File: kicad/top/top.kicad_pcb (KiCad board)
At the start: 2 copper layers, 65 x 120 mm, 32 parts, among them J1 OLED_128x64, J2 Conn_01x15, SW1 SLW-864574-5A-RA-N-D, SW2 RotaryEncoder_Switch

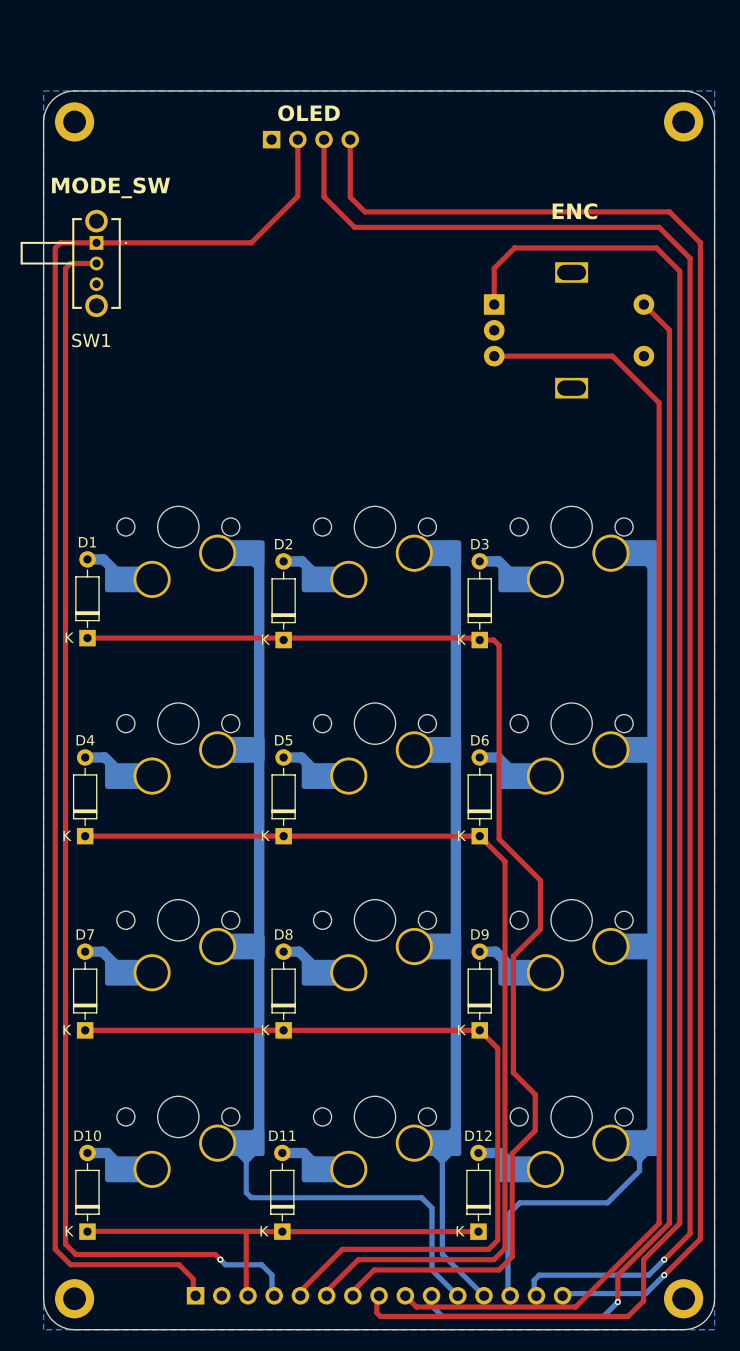
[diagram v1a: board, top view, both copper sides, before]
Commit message: Changed from Adafruit Feather V2 to UnkownMaker ProS3 [D] for USB HID feature. Changed OLED from 128x64 to 128x32
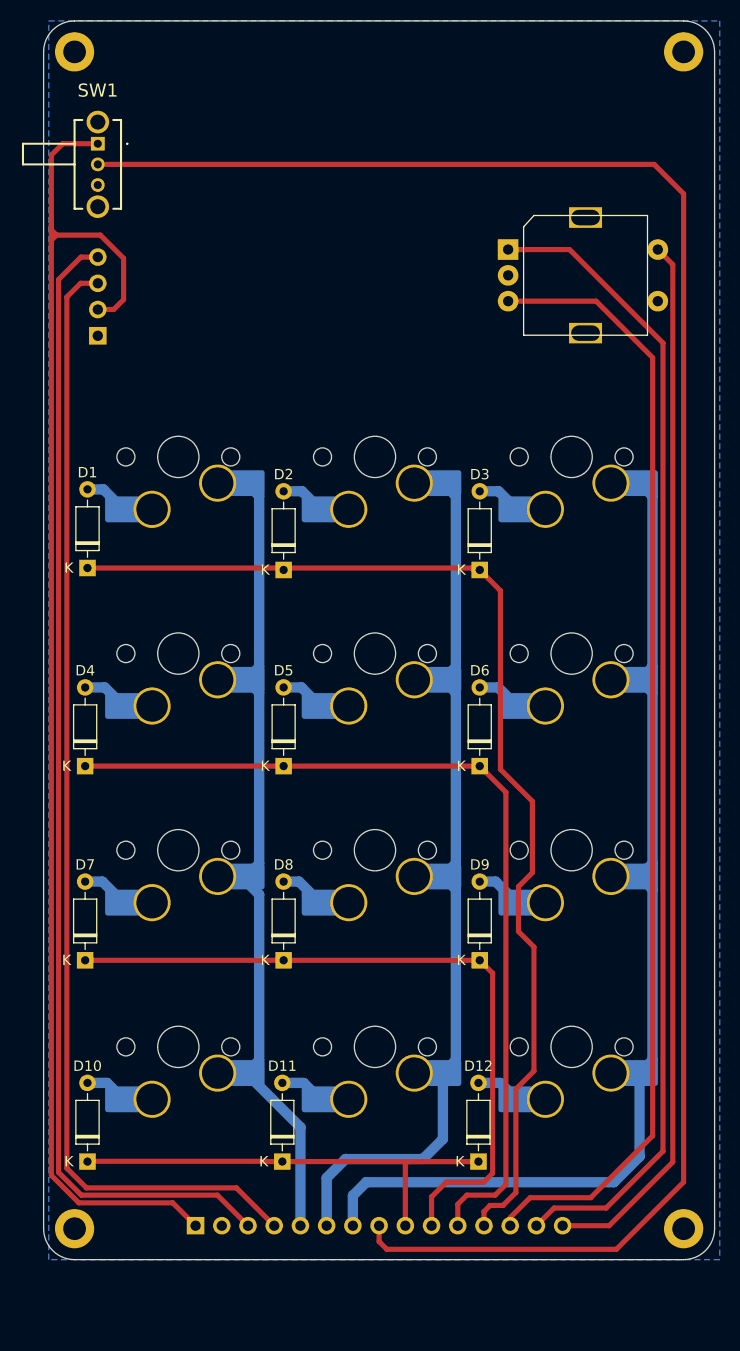
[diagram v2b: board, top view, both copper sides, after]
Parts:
- J1: value OLED_128x64 -> OLED_128x32; footprint Project-Footprints:OLED_128x64 -> ScottoKeebs_Components:OLED_128x32
- moved J1 24.1 mm to (16.4, 33.8)
- moved SW1 9.60 mm to (18.0, 25.0)
- moved H3 6.79 mm to (15.8, 130.1)
- moved H4 6.79 mm to (74.8, 130.1)
- moved D10 6.79 mm to (17.0, 123.6)
- moved D11 6.79 mm to (35.9, 123.6)
- moved D12 6.79 mm to (54.9, 123.6)
- moved S10 6.79 mm to (26.5, 116.3)
- moved S11 6.79 mm to (45.5, 116.3)
- moved S12 6.79 mm to (64.6, 116.3)
- moved S7 6.79 mm to (26.5, 97.3)
- moved S8 6.79 mm to (45.5, 97.3)
- moved S9 6.79 mm to (64.6, 97.3)
- moved H1 6.79 mm to (74.8, 16.1)
- moved H2 6.79 mm to (15.8, 16.1)
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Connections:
- J2 pad 10: ENC_SW -> ROW2
- J2 pad 11: COL0 -> ROW1
- J2 pad 12: COL1 -> ROW0
- J2 pad 13: COL2 -> ENC_DT
- J2 pad 14: OLED_SCL -> ENC_CLK
- J2 pad 15: OLED_SDA -> ENC_SW
- J2 pad 3: ROW3 -> OLED_SDA
- J2 pad 4: BT_SELECT -> OLED_SCL
- J2 pad 5: ROW2 -> COL0
- J2 pad 6: ROW1 -> COL1
- J2 pad 7: ROW0 -> COL2
- J2 pad 8: ENC_CLK -> BT_SELECT
- J2 pad 9: ENC_DT -> ROW3
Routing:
- net BT_SELECT: track 120.7 -> 187.7 mm, vias 1 -> 0
- net OLED_SCL: track 156.2 -> 110.3 mm, vias 1 -> 0
- net OLED_SDA: track 153.6 -> 112.7 mm, vias 1 -> 0
- net ENC_CLK: track 152.9 -> 112.3 mm
- net COL0: track 96.4 -> 76.7 mm
- net ENC_SW: track 120.0 -> 102.2 mm, vias 1 -> 0
- net ENC_DT: track 126.0 -> 109.5 mm
- net ROW0: track 121.1 -> 107.6 mm
- net COL2: track 87.4 -> 100.6 mm
- net ROW2: track 80.8 -> 69.0 mm
- net ROW1: track 98.5 -> 87.3 mm
- net +3.3V: track 144.0 -> 137.0 mm
- net ROW3: track 43.9 -> 51.0 mm
- net COL1: track 77.2 -> 84.1 mm
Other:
- board text removed: "ENC"
- board text removed: "MODE_SW"
- board text removed: "OLED"

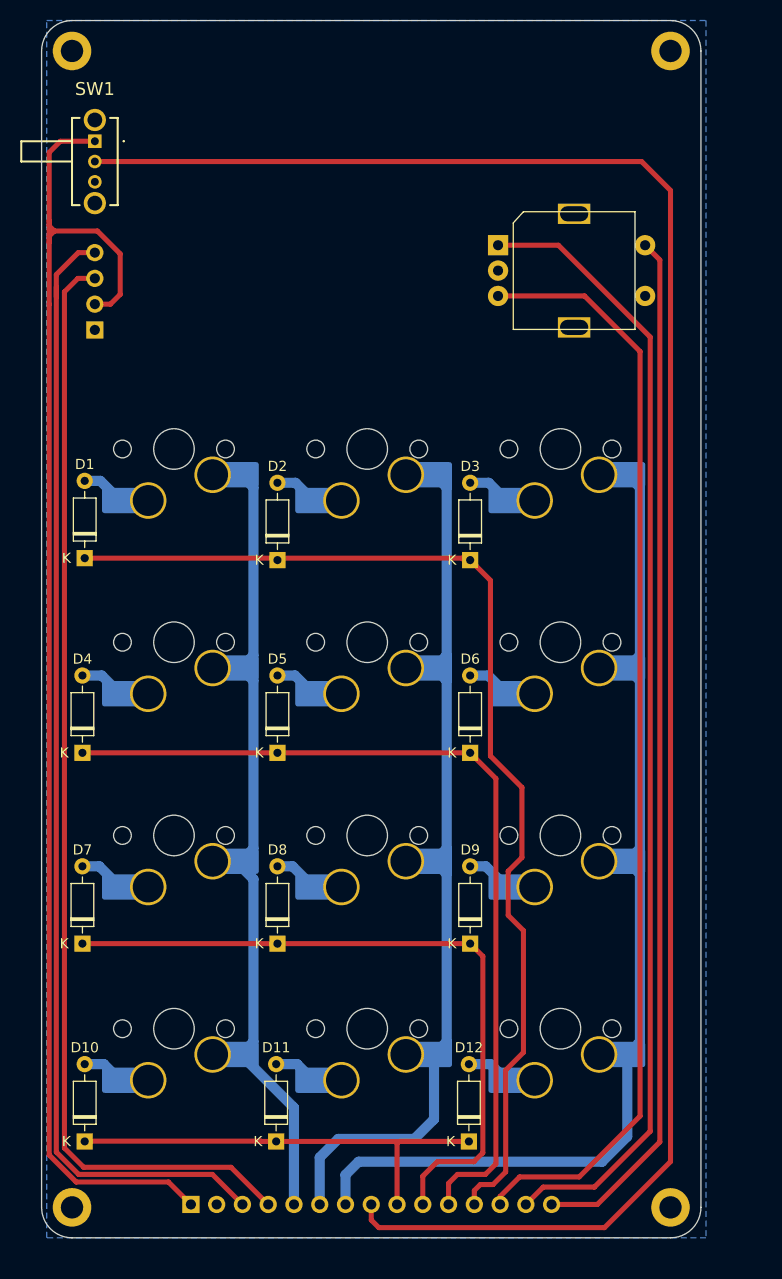
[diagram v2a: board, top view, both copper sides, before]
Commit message: added visuals, updated the documentation
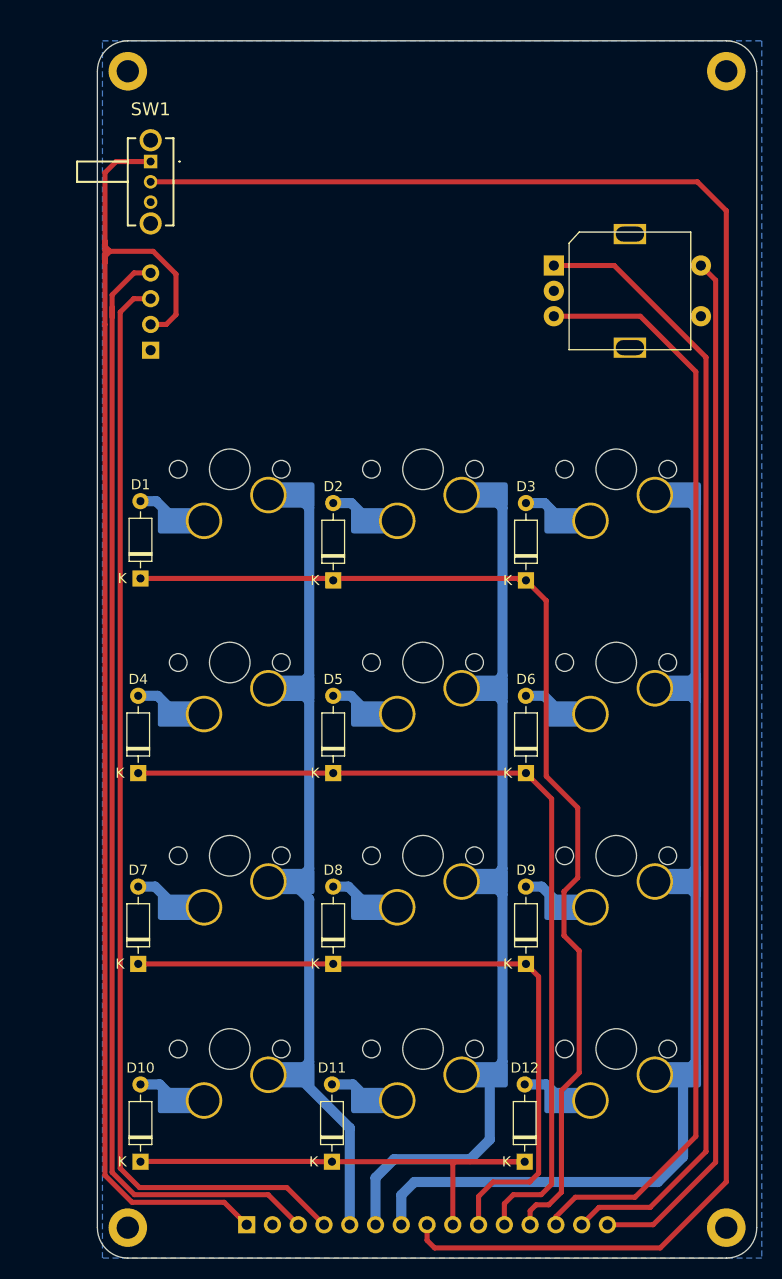
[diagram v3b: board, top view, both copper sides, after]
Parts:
- moved D1 5.85 mm to (22.5, 68.1)
- moved D10 5.85 mm to (22.5, 125.6)
- moved D11 5.85 mm to (41.4, 125.6)
- moved D12 5.85 mm to (60.4, 125.6)
- moved D2 5.85 mm to (41.5, 68.3)
- moved D3 5.85 mm to (60.5, 68.3)
- moved D4 5.85 mm to (22.3, 87.3)
- moved D5 5.85 mm to (41.5, 87.3)
- moved D6 5.85 mm to (60.5, 87.3)
- moved D7 5.85 mm to (22.3, 106.1)
- moved D8 5.85 mm to (41.5, 106.1)
- moved D9 5.85 mm to (60.5, 106.1)
- moved H1 5.85 mm to (80.3, 18.1)
- moved H2 5.85 mm to (21.3, 18.1)
- moved H3 5.85 mm to (21.3, 132.1)
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
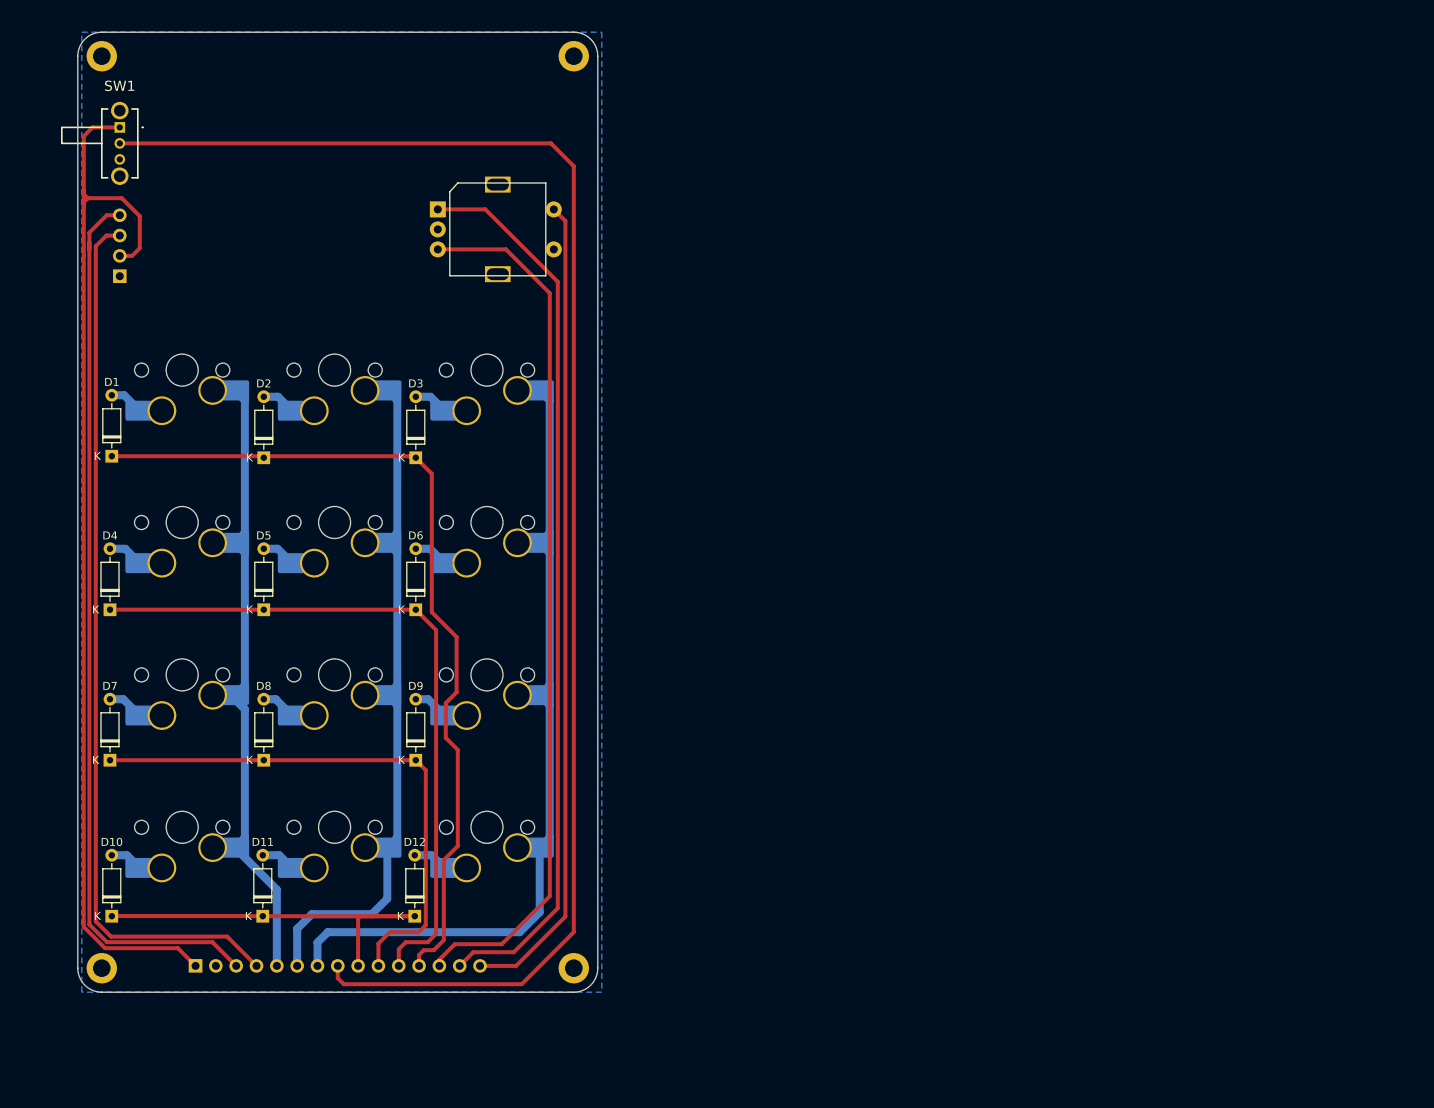
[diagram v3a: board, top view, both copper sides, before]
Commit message: update imports, readme, documentatie, add 10 addressable rgbs
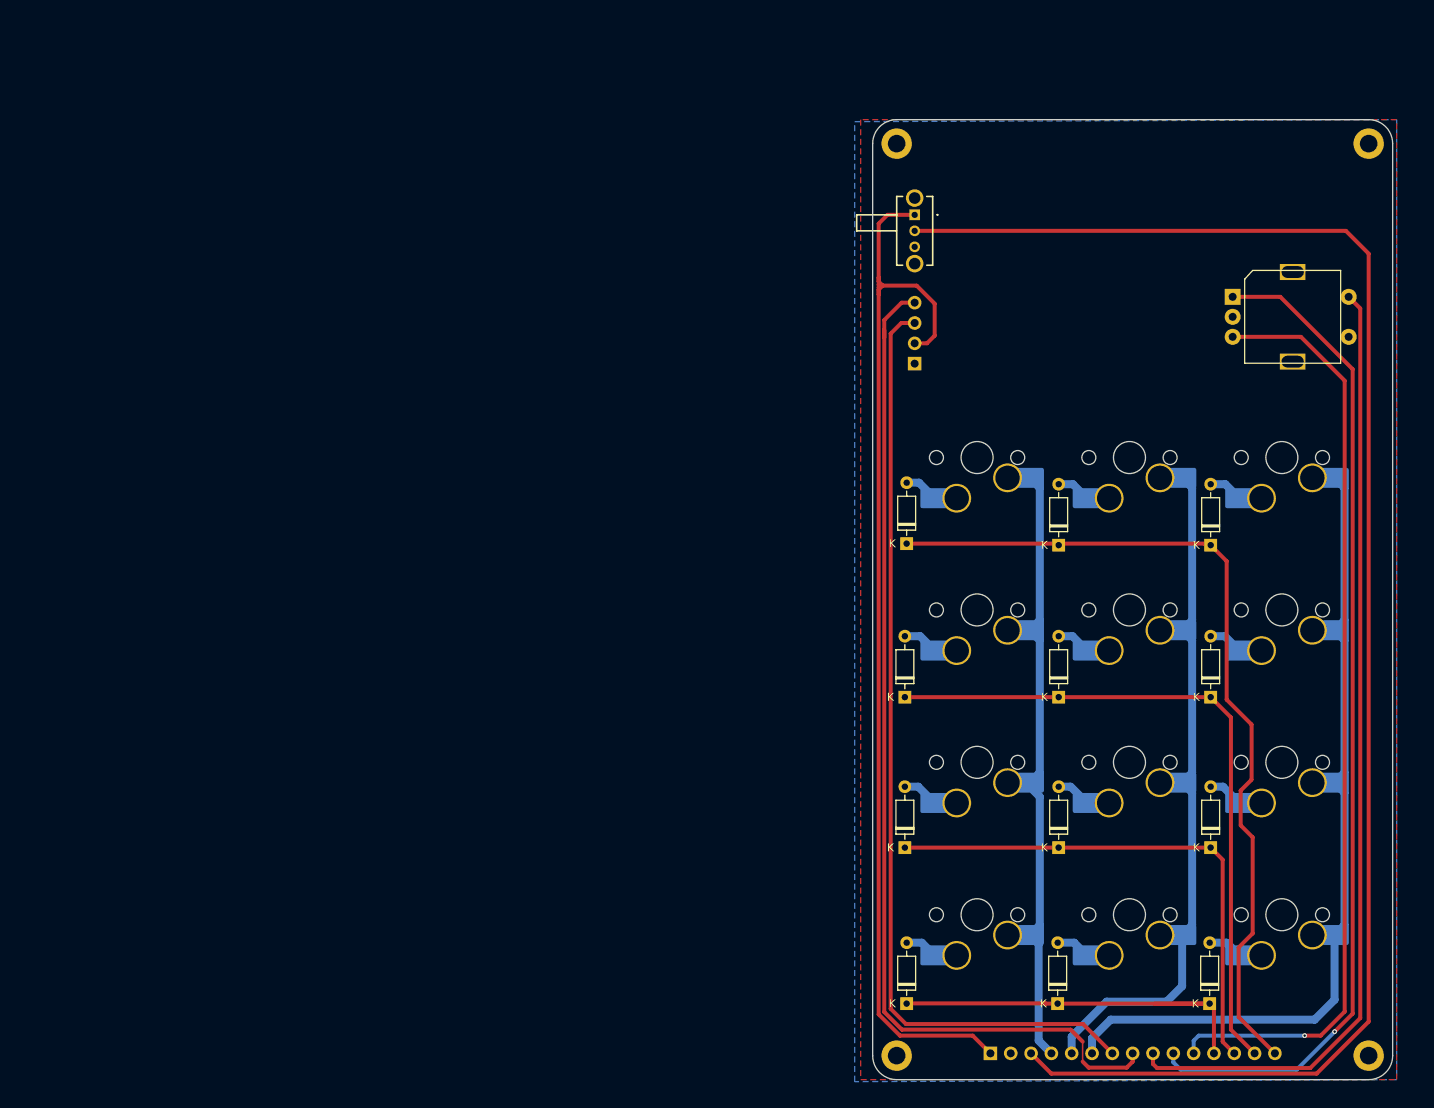
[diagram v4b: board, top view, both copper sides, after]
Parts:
- added G***: LOGO, Project-Footprints:nubcat_10mm, B.Cu at (139.7, 36.1)
- added G***: LOGO, Project-Footprints:nubcat4_24mm, B.Cu at (152.2, 37.6)
- D1, D10, D11, D12, D2, D3, D4, D5, D6, D7, D8, D9: footprint Project-Footprints:D_DO-35_SOD27_P7.62mm_Horizontal -> Top-Footprints:D_DO-35_SOD27_P7.62mm_Horizontal
- H1, H2, H3, H4: footprint Project-Footprints:MountingHole_2.2mm_M2_DIN965_Pad -> Top-Footprints:MountingHole_2.2mm_M2_DIN965_Pad
- J1: footprint ScottoKeebs_Components:OLED_128x32 -> Top-Footprints:OLED_128x32
- J2: footprint Project-Footprints:PinHeader_1x15_P2.54mm_Vertical -> Top-Footprints:PinHeader_1x15_P2.54mm_Vertical
- S1, S10, S11, S12, S2, S3, S4, S5, S6, S7, S8, S9: footprint Project-Footprints:MX_Hotswap_1.00u -> Top-Footprints:MX_Hotswap_1.00u
- SW1: footprint Project-Footprints:SLW8645745ARAND -> Top-Footprints:SLW8645745ARAND
- SW2: footprint Project-Footprints:Encoder_EC11_MX -> Top-Footprints:Encoder_EC11_MX
- moved S11 100.0 mm to (150.4, 129.3)
- moved S2 100.0 mm to (150.4, 72.1)
- moved S5 100.0 mm to (150.4, 91.2)
- moved S8 100.0 mm to (150.4, 110.2)
- moved D1 100.0 mm to (121.9, 79.1)
- moved D10 100.0 mm to (121.9, 136.6)
- moved D11 100.0 mm to (140.8, 136.6)
- moved D12 100.0 mm to (159.8, 136.6)
- moved D2 100.0 mm to (140.9, 79.3)
- moved D3 100.0 mm to (159.9, 79.3)
- moved D4 100.0 mm to (121.7, 98.3)
- moved D5 100.0 mm to (140.9, 98.3)
- moved D6 100.0 mm to (159.9, 98.3)
- moved D7 100.0 mm to (121.7, 117.1)
- moved D8 100.0 mm to (140.9, 117.1)
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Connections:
- J2 pad 10: ROW2 -> ENC_CLK
- J2 pad 11: ROW1 -> ENC_DT
- J2 pad 12: ROW0 -> ROW3
- J2 pad 13: ENC_DT -> ROW2
- J2 pad 14: ENC_CLK -> ROW1
- J2 pad 15: ENC_SW -> ROW0
- J2 pad 3: OLED_SDA -> BT_SELECT
- J2 pad 4: OLED_SCL -> COL0
- J2 pad 5: COL0 -> COL1
- J2 pad 6: COL1 -> COL2
- J2 pad 7: COL2 -> OLED_SCL
- J2 pad 8: BT_SELECT -> OLED_SDA
- J2 pad 9: ROW3 -> ENC_SW
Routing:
- net ENC_SW: track 102.2 -> 120.8 mm
- net OLED_SDA: track 112.7 -> 128.9 mm
- net ENC_CLK: track 112.3 -> 126.1 mm, vias 0 -> 1
- net BT_SELECT: track 187.7 -> 199.9 mm
- net OLED_SCL: track 110.3 -> 118.0 mm
- net ENC_DT: track 109.5 -> 117.1 mm, vias 0 -> 1
- net ROW2: track 69.0 -> 65.2 mm
- net ROW1: track 87.3 -> 85.0 mm
- net COL2: track 100.6 -> 102.5 mm
- net COL1: track 84.1 -> 85.2 mm
- net COL0: track 76.7 -> 75.7 mm
- added copper zone on F.Cu, net GND
